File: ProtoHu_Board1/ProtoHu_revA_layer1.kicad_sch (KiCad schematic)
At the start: 8 parts, among them IC1 SST39SF040-45-4C-WHE-T, IC2 74LS32, J1 HUCARD-EDGE, J2 SST39SF040-70-4C-PHE

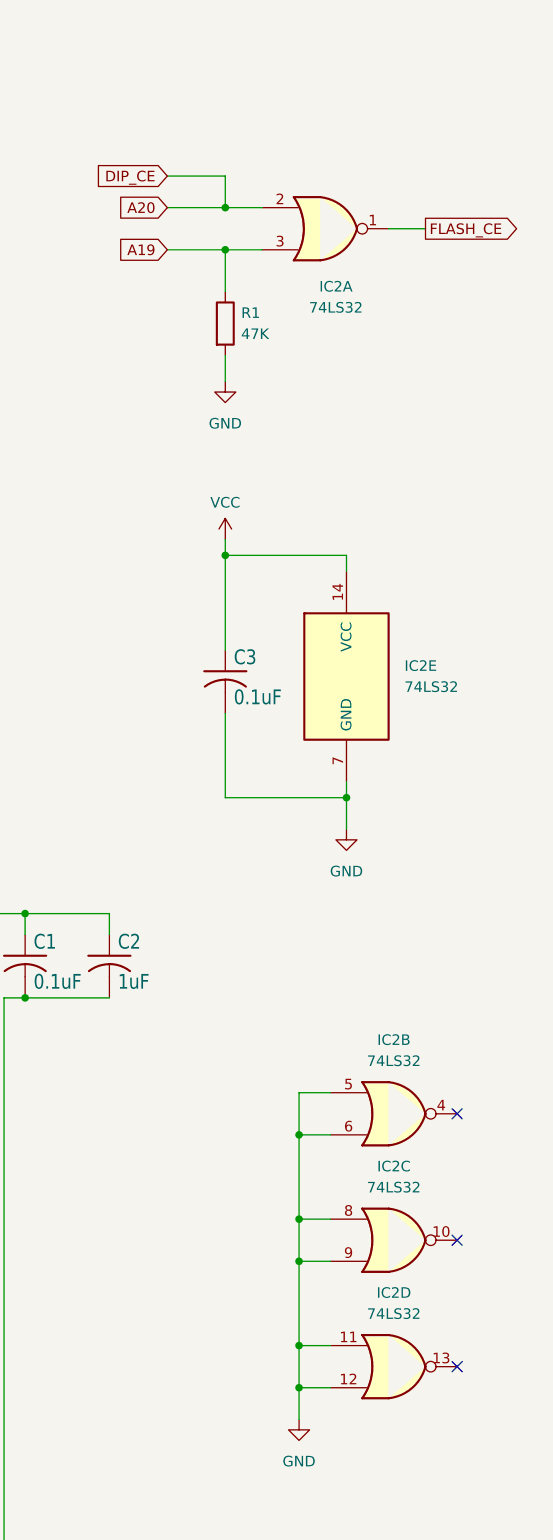
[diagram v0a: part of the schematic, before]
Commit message: Fix pinout and part (LS -> HC) for IC2.
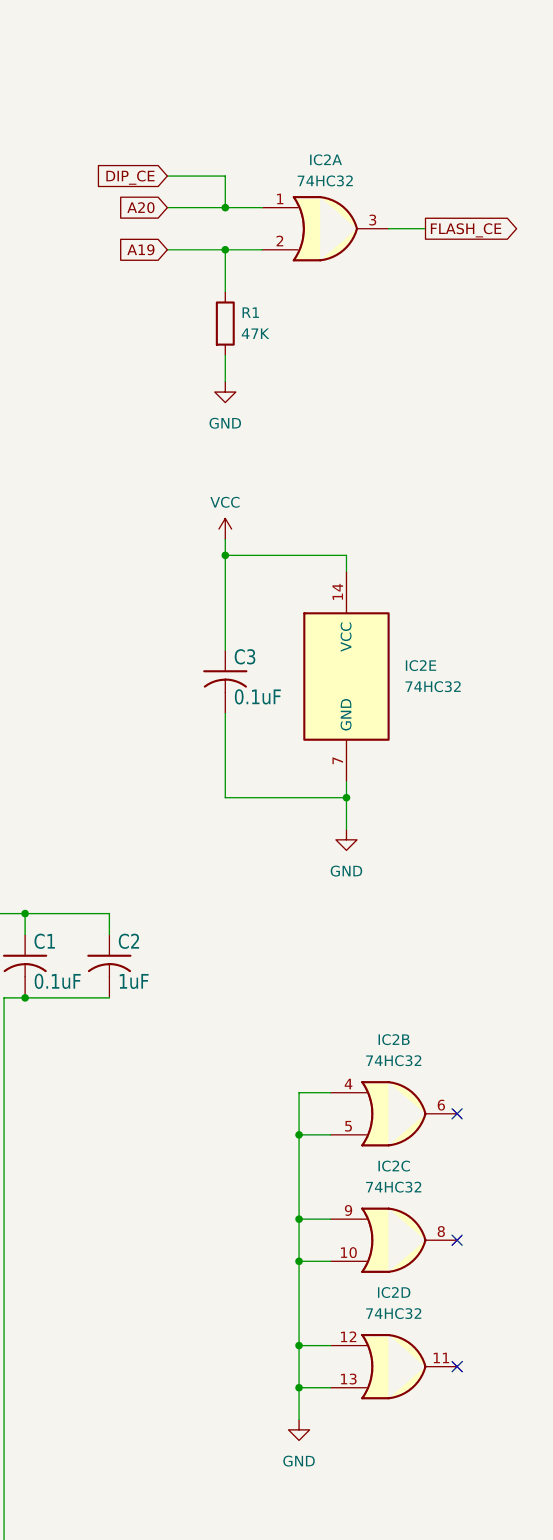
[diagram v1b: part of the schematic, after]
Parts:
- removed IC2: 74LS32, ProtoHu_revA_layer1:TSSOP-14_4.4x5mm_P0.65mm, symbol 74xx:74LS02
- added IC2: 74HC32, ProtoHu_revA_layer1:TSSOP-14_4.4x5mm_P0.65mm, symbol 74xx:74LS32
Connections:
- net A19: now also IC2.2
- net A20: now also IC2.1
- net FLASH_CE: now also IC2.3
- net GND: now also IC2.10, IC2.12, IC2.13, IC2.4, IC2.5, IC2.7 (GND), IC2.9
- net VCC: now also IC2.14 (VCC)
